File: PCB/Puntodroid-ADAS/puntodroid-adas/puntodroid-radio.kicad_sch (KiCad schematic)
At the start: 3 parts, among them U10 RFM69HCW

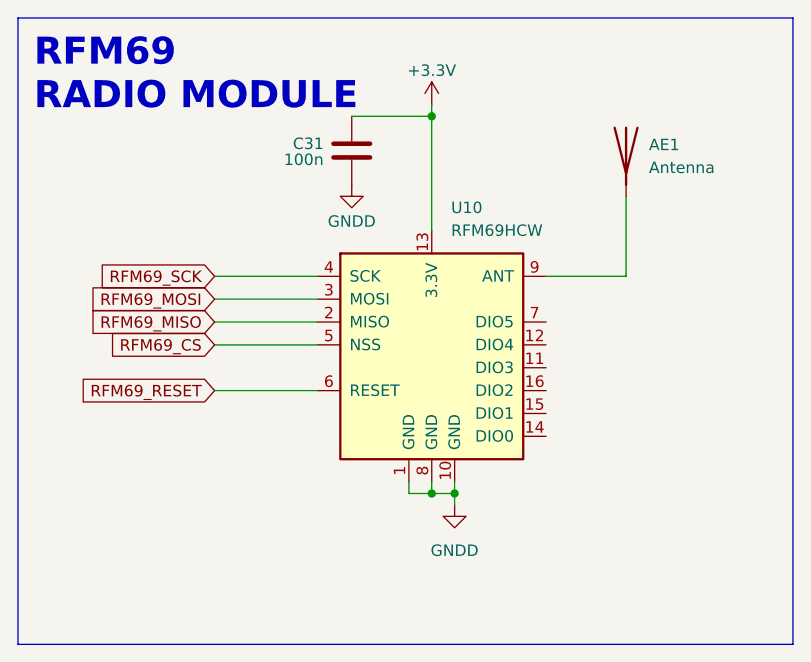
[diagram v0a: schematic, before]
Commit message: move to kicad v10. change rfm69 to lora radio, add push button connector, add puntodroid logo
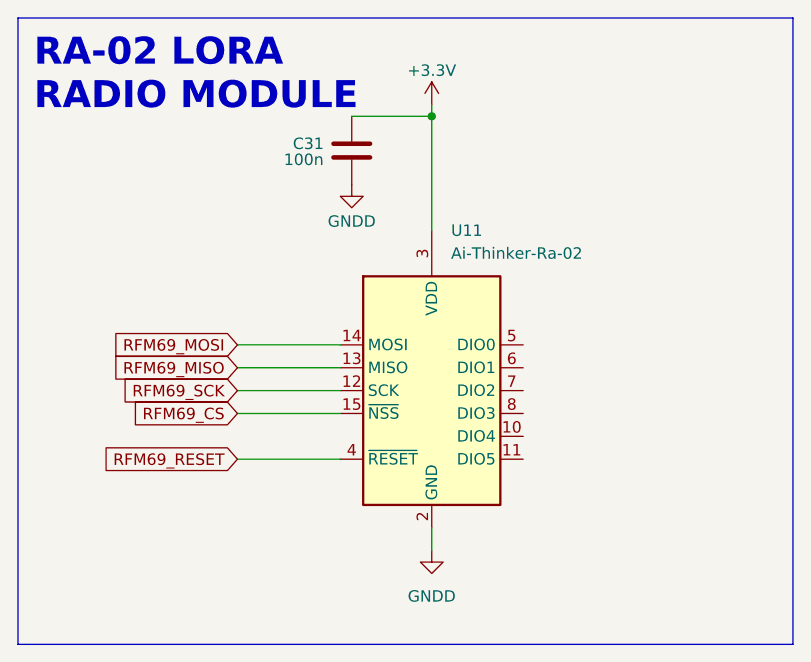
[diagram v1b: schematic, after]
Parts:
- removed AE1: Antenna, Capacitor_SMD:C_0805_2012Metric_Pad1.18x1.45mm_HandSolder, symbol Device:Antenna
- removed U10: RFM69HCW, RF_Module:HOPERF_RFM69HW, symbol RF_Module:RFM69HCW
- added U11: Ai-Thinker-Ra-02, RF_Module:Ai-Thinker-Ra-01-LoRa, symbol RF_Module:Ai-Thinker-Ra-02
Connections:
- net +3.3V: now also U11.3 (VDD)
- net GNDD: now also U11.1 (GND), U11.16 (GND), U11.2 (GND), U11.9 (GND)
- net RFM69_CS: now also U11.15 (~{NSS})
- net RFM69_MISO: now also U11.13 (MISO)
- net RFM69_MOSI: now also U11.14 (MOSI)
- net RFM69_RESET: now also U11.4 (~{RESET})
- net RFM69_SCK: now also U11.12 (SCK)
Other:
- note added: "RA-02 LORA RADIO MODULE"
- note removed: "RFM69 RADIO MODULE"
